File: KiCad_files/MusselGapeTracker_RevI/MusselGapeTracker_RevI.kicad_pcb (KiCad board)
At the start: 2 copper layers, 72.5 x 57.8 mm, 83 parts, among them J1 AVR_SPI_PRG_6PTH, U1 ATMEGA328P, U2 DS3231M+TRL, U3 DS3231MZ

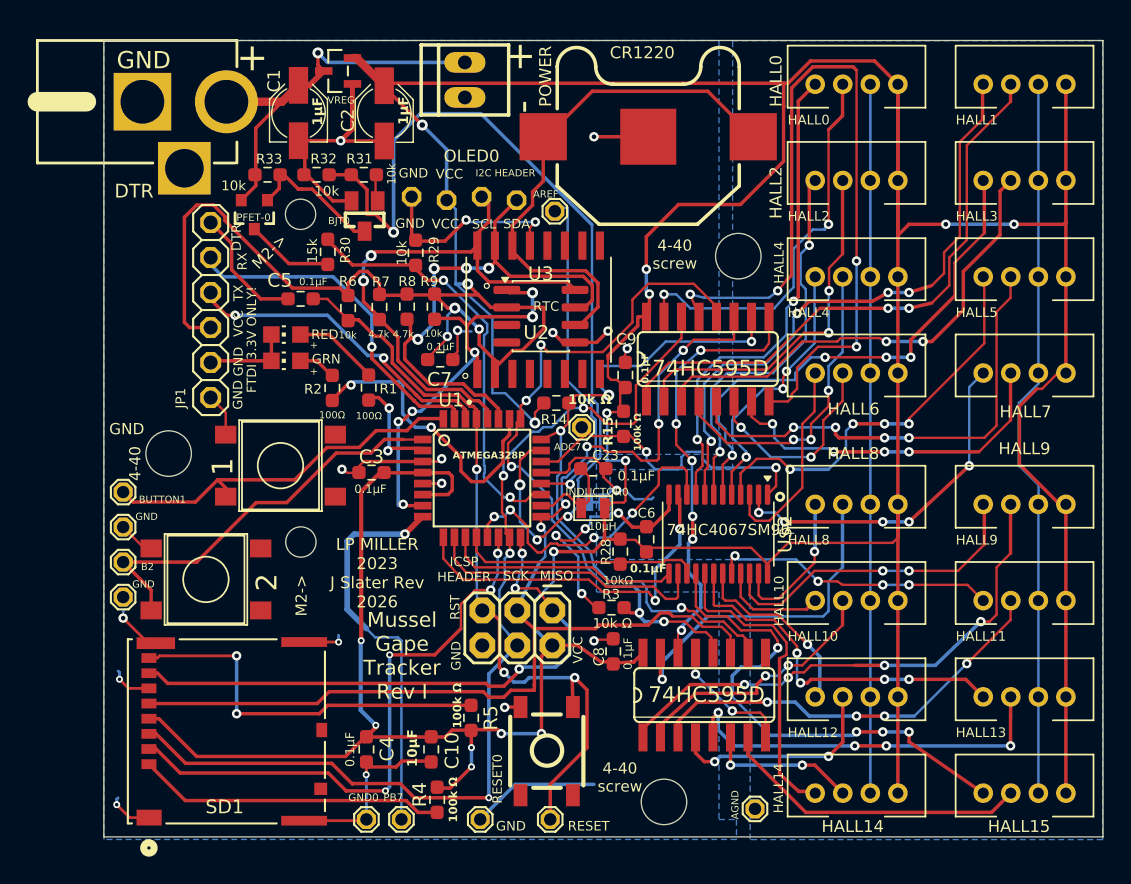
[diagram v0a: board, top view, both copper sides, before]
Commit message: Fixed SD card mount traces
Ran SD card traces on bottom instead of top to avoid sd mount prohibition area
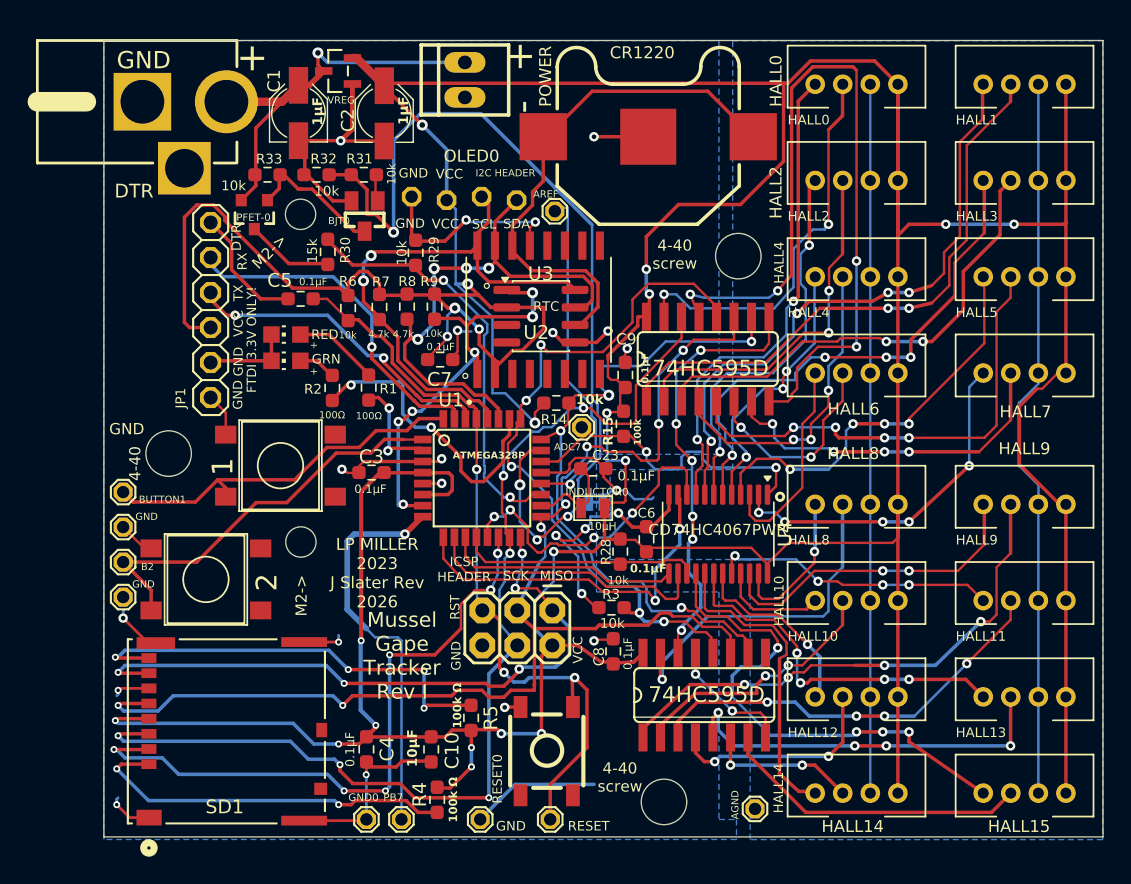
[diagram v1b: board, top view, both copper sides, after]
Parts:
- MOLEX_KK0: value >VALUE -> 22-23-2021
- R1, R2: value 100 Ω -> 100
- R14, R3, R6, R9: value 10k Ω -> 10k
- R15, R4, R5: value 100k Ω -> 100k
- R28: value 10kΩ -> 10k
- U4: renamed from U$2; value 74HC4067SM96 -> CD74HC4067PWR
- renumbered MCP1700T-3302 to MCP1700T3302
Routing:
- net /SCK: track 86.6 -> 92.1 mm, vias 5 -> 7
- net /CS_SD: track 42.7 -> 47.8 mm, vias 4 -> 6
- net /MISO: track 43.0 -> 48.0 mm, vias 3 -> 5
- net Net-(SD1-DAT2): track 22.4 -> 27.3 mm, vias 0 -> 2
- net /MOSI: track 73.6 -> 78.3 mm, vias 4 -> 6
- net VCC: track 429.1 -> 433.3 mm, vias 19 -> 21
- net Net-(SD1-DAT1): track 28.1 -> 31.9 mm, vias 2 -> 4
